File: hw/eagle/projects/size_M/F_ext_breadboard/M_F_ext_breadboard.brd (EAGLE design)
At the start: 10 parts

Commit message: pcb M.1 -not finished
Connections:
- net GND: now also JP11.4; no longer JP11.3
- net VDD: now also JP11.3; no longer JP11.4
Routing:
- net GND: track 26.6 -> 29.3 mm
- net VDD: track 0.00 -> 1.83 mm
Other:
- board text added: "breadbrd M.1"
- board text removed: "bredboard M.0"

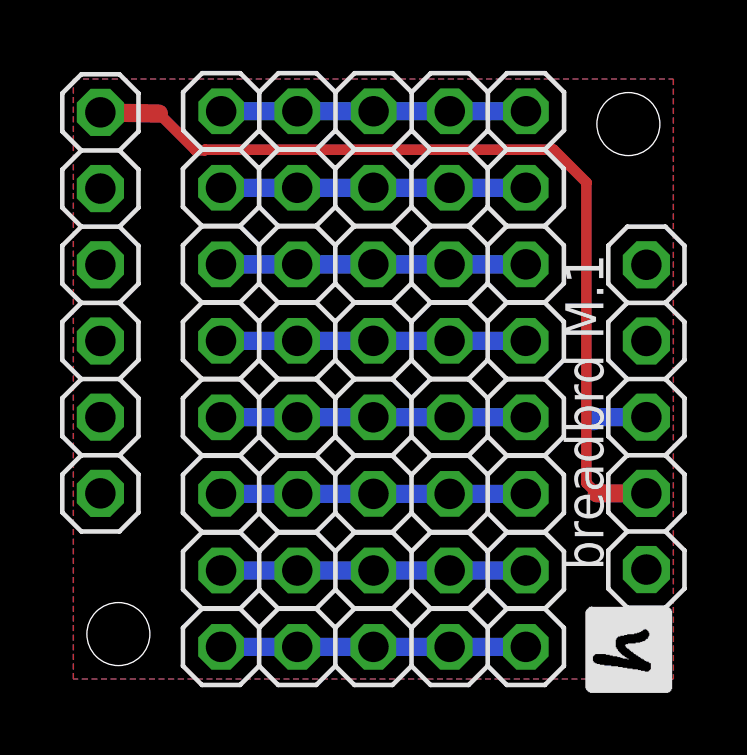
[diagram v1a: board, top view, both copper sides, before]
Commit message: updateed PCBs - adjustments based on usage of version 1
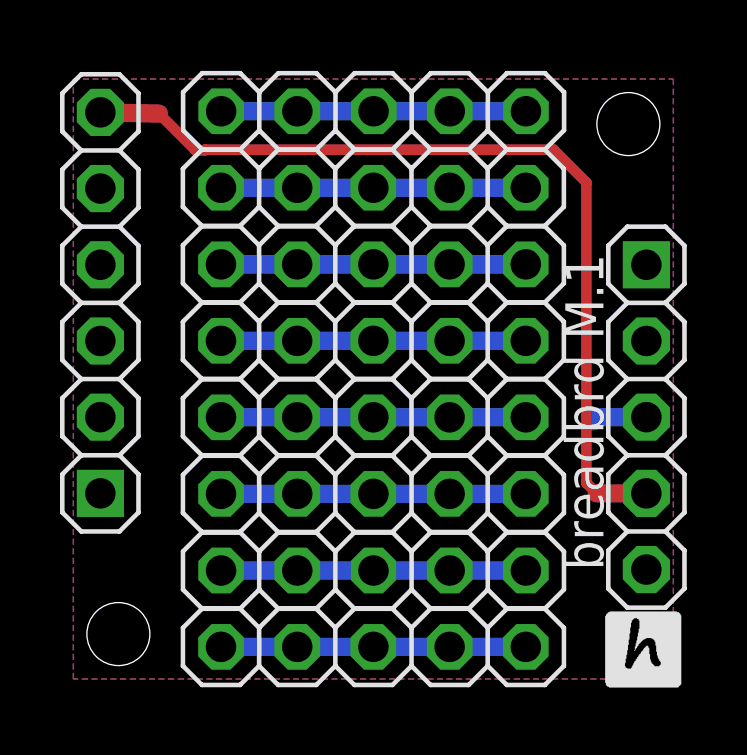
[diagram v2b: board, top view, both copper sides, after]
